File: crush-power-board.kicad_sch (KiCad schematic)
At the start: 0 parts

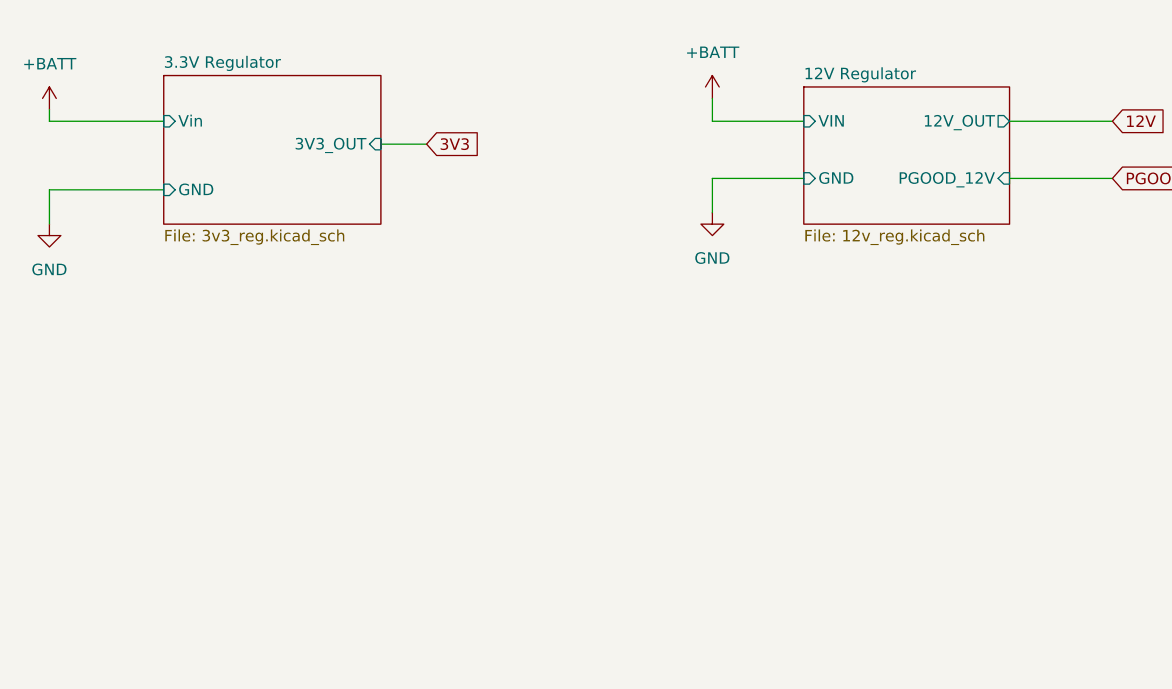
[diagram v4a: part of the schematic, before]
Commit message: Changed 12V Regulator values, added thruster side 3V3 regulator
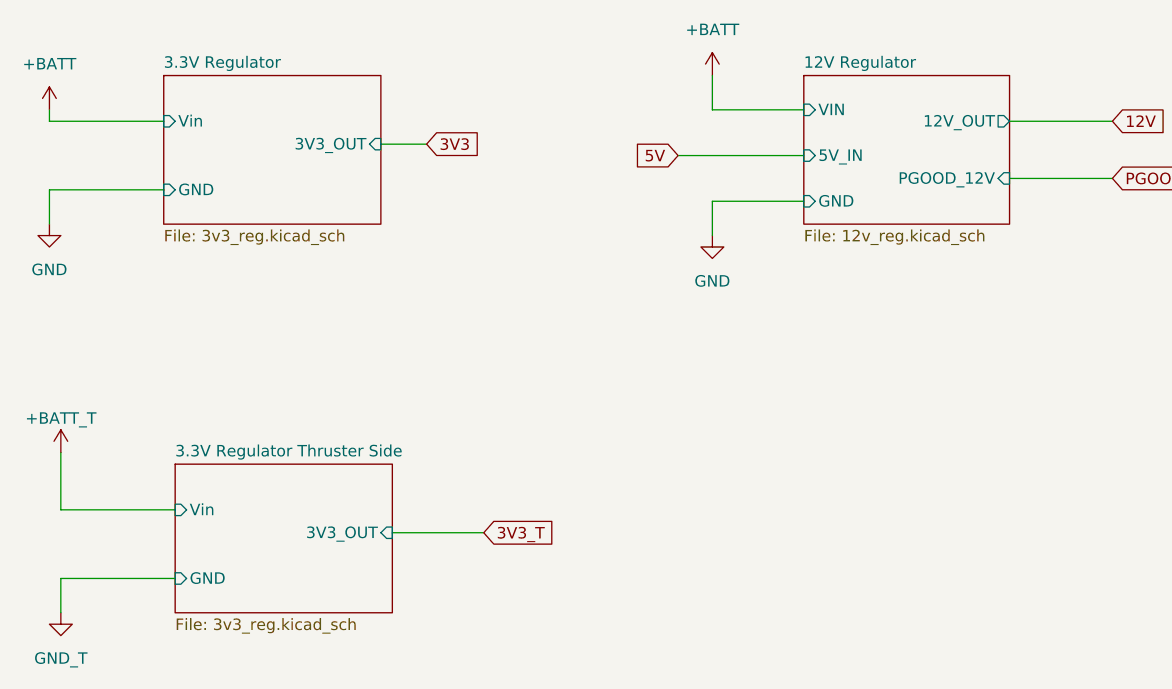
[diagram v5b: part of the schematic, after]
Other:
- added sheet 3.3V Regulator Thruster Side (3v3_reg.kicad_sch)
- sheet 12V Regulator ports: added 5V_IN; removed none
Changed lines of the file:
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@@
     (stroke (width 0) (type default))
   )
-  (wire (pts (xy 142.24 34.29) (xy 132.08 34.29))
+  (wire (pts (xy 142.24 33.02) (xy 132.08 33.02))
     (stroke (width 0) (type default))
   )
@@
     (stroke (width 0) (type default))
   )
-  (wire (pts (xy 132.08 40.64) (xy 132.08 44.45))
+  (wire (pts (xy 59.69 77.47) (xy 72.39 77.47))
+    (stroke (width 0) (type default))
+  )
+  (wire (pts (xy 132.08 43.18) (xy 132.08 46.99))
+    (stroke (width 0) (type default))
+  )
+  (wire (pts (xy 59.69 71.12) (xy 59.69 77.47))
     (stroke (width 0) (type default))
   )
@@
     (stroke (width 0) (type default))
   )
+  (wire (pts (xy 96.52 80.01) (xy 106.68 80.01))
+    (stroke (width 0) (type default))
+  )
+  (wire (pts (xy 59.69 85.09) (xy 59.69 88.9))
+    (stroke (width 0) (type default))
+  )
   (wire (pts (xy 58.42 34.29) (xy 71.12 34.29))
     (stroke (width 0) (type default))
   )
-  (wire (pts (xy 132.08 40.64) (xy 142.24 40.64))
-    (stroke (width 0) (type default))
-  )
-  (wire (pts (xy 132.08 31.75) (xy 132.08 34.29))
+  (wire (pts (xy 132.08 43.18) (xy 142.24 43.18))
+    (stroke (width 0) (type default))
+  )
+  (wire (pts (xy 72.39 85.09) (xy 59.69 85.09))
+    (stroke (width 0) (type default))
+  )
+  (wire (pts (xy 128.27 38.1) (xy 142.24 38.1))
+    (stroke (width 0) (type default))
+  )
+  (wire (pts (xy 132.08 29.21) (xy 132.08 33.02))
     (stroke (width 0) (type default))
   )
@@
     )
   )
+  (global_label "3V3_T" (shape input) (at 106.68 80.01 0) (fields_autoplaced)
+    (effects (font (size 1.27 1.27)) (justify left))
+    (property "Intersheetrefs" "${INTERSHEET_REFS}" (at 115.0286 80.01 0)
+      (effects (font (size 1.27 1.27)) (justify left) hide)
+    )
+  )
   (global_label "3V3" (shape input) (at 100.33 36.83 0) (fields_autoplaced)
     (effects (font (size 1.27 1.27)) (justify left))
@@
     )
   )
+  (global_label "5V" (shape input) (at 128.27 38.1 180) (fields_autoplaced)
+    (effects (font (size 1.27 1.27)) (justify right))
+    (property "Intersheetrefs" "${INTERSHEET_REFS}" (at 123.0661 38.1 0)
+      (effects (font (size 1.27 1.27)) (justify right) hide)
+    )
+  )
   (symbol (lib_id "power:GND") (at 58.42 45.72 0) (unit 1)
     (in_bom yes) (on_board yes) (dnp no) (fields_autoplaced)
@@
     )
   )
-  (symbol (lib_id "power:GND") (at 132.08 44.45 0) (unit 1)
-    (in_bom yes) (on_board yes) (dnp no) (fields_autoplaced)
-    (property "Reference" "#PWR04" (at 132.08 50.8 0)
-      (effects (font (size 1.27 1.27)) hide)
-    )
-    (property "Value" "GND" (at 132.08 49.53 0)
-      (effects (font (size 1.27 1.27)))
-    )
-    (property "Footprint" "" (at 132.08 44.45 0)
-      (effects (font (size 1.27 1.27)) hide)
-    )
-    (property "Datasheet" "" (at 132.08 44.45 0)
+  (symbol (lib_id "power:GND") (at 132.08 46.99 0) (unit 1)
+    (in_bom yes) (on_board yes) (dnp no) (fields_autoplaced)
+    (property "Reference" "#PWR04" (at 132.08 53.34 0)
+      (effects (font (size 1.27 1.27)) hide)
+    )
+    (property "Value" "GND" (at 132.08 52.07 0)
+      (effects (font (size 1.27 1.27)))
+    )
+    (property "Footprint" "" (at 132.08 46.99 0)
+      (effects (font (size 1.27 1.27)) hide)
+    )
+    (property "Datasheet" "" (at 132.08 46.99 0)
       (effects (font (size 1.27 1.27)) hide)
     )
@@
     )
   )
-  (symbol (lib_id "power:+BATT") (at 132.08 31.75 0) (unit 1)
-    (in_bom yes) (on_board yes) (dnp no) (fields_autoplaced)
-    (property "Reference" "#PWR03" (at 132.08 35.56 0)
-      (effects (font (size 1.27 1.27)) hide)
-    )
-    (property "Value" "+BATT" (at 132.08 26.67 0)
-      (effects (font (size 1.27 1.27)))
-    )
-    (property "Footprint" "" (at 132.08 31.75 0)
-      (effects (font (size 1.27 1.27)) hide)
-    )
-    (property "Datasheet" "" (at 132.08 31.75 0)
+  (symbol (lib_id "power:+BATT") (at 132.08 29.21 0) (unit 1)
+    (in_bom yes) (on_board yes) (dnp no) (fields_autoplaced)
+    (property "Reference" "#PWR03" (at 132.08 33.02 0)
+      (effects (font (size 1.27 1.27)) hide)
+    )
+    (property "Value" "+BATT" (at 132.08 24.13 0)
+      (effects (font (size 1.27 1.27)))
+    )
+    (property "Footprint" "" (at 132.08 29.21 0)
+      (effects (font (size 1.27 1.27)) hide)
+    )
+    (property "Datasheet" "" (at 132.08 29.21 0)
       (effects (font (size 1.27 1.27)) hide)
     )
@@
         (path "/530b9f5d-4c5f-47a4-a889-3cce870d311f"
           (reference "#PWR03") (unit 1)
+        )
+      )
+    )
+  )
+  (symbol (lib_id "power:+BATT") (at 59.69 71.12 0) (unit 1)
+    (in_bom yes) (on_board yes) (dnp no) (fields_autoplaced)
+    (property "Reference" "#PWR07" (at 59.69 74.93 0)
+      (effects (font (size 1.27 1.27)) hide)
+    )
+    (property "Value" "+BATT_T" (at 59.69 67.31 0)
+      (effects (font (size 1.27 1.27)))
+    )
+    (property "Footprint" "" (at 59.69 71.12 0)
+      (effects (font (size 1.27 1.27)) hide)
+    )
+    (property "Datasheet" "" (at 59.69 71.12 0)
+      (effects (font (size 1.27 1.27)) hide)
+    )
+    (pin "1")
+    (instances
+      (project "crush-power-board"
+        (path "/530b9f5d-4c5f-47a4-a889-3cce870d311f"
+          (reference "#PWR07") (unit 1)
+        )
+      )
+    )
+  )
+  (symbol (lib_id "power:GND") (at 59.69 88.9 0) (unit 1)
+    (in_bom yes) (on_board yes) (dnp no) (fields_autoplaced)
+    (property "Reference" "#PWR08" (at 59.69 95.25 0)
+      (effects (font (size 1.27 1.27)) hide)
+    )
+    (property "Value" "GND_T" (at 59.69 93.98 0)
+      (effects (font (size 1.27 1.27)))
+    )
+    (property "Footprint" "" (at 59.69 88.9 0)
+      (effects (font (size 1.27 1.27)) hide)
+    )
+    (property "Datasheet" "" (at 59.69 88.9 0)
+      (effects (font (size 1.27 1.27)) hide)
+    )
+    (pin "1")
+    (instances
+      (project "crush-power-board"
+        (path "/530b9f5d-4c5f-47a4-a889-3cce870d311f"
+          (reference "#PWR08") (unit 1)
         )
       )
@@
     )
   )
-  (sheet (at 142.24 30.48) (size 22.86 15.24) (fields_autoplaced)
+  (sheet (at 142.24 29.21) (size 22.86 16.51) (fields_autoplaced)
     (stroke (width 0.1524) (type solid))
     (fill (color 0 0 0 0.0000))
-    (property "Sheetname" "12V Regulator" (at 142.24 29.7684 0)
+    (property "Sheetname" "12V Regulator" (at 142.24 28.4984 0)
       (effects (font (size 1.27 1.27)) (justify left bottom))
     )
@@
       (effects (font (size 1.27 1.27)) (justify right))
     )
-    (pin "GND" input (at 142.24 40.64 180)
-      (effects (font (size 1.27 1.27)) (justify left))
-    )
-    (pin "VIN" input (at 142.24 34.29 180)
+    (pin "GND" input (at 142.24 43.18 180)
+      (effects (font (size 1.27 1.27)) (justify left))
+    )
+    (pin "VIN" input (at 142.24 33.02 180)
       (effects (font (size 1.27 1.27)) (justify left))
     )
@@
       (effects (font (size 1.27 1.27)) (justify right))
     )
+    (pin "5V_IN" input (at 142.24 38.1 180)
+      (effects (font (size 1.27 1.27)) (justify left))
+    )
     (instances
       (project "crush-power-board"
@@
       )
     )
+  )
+  (sheet (at 72.39 72.39) (size 24.13 16.51) (fields_autoplaced)
+    (stroke (width 0.1524) (type solid))
+    (fill (color 0 0 0 0.0000))
+    (property "Sheetname" "3.3V Regulator Thruster Side" (at 72.39 71.6784 0)
+      (effects (font (size 1.27 1.27)) (justify left bottom))
+    )
+    (property "Sheetfile" "3v3_reg.kicad_sch" (at 72.39 89.4846 0)
+      (effects (font (size 1.27 1.27)) (justify left top))
+    )
+    (pin "GND" input (at 72.39 85.09 180)
+      (effects (font (size 1.27 1.27)) (justify left))
+    )
+    (pin "Vin" input (at 72.39 77.47 180)
+      (effects (font (size 1.27 1.27)) (justify left))
+    )
+    (pin "3V3_OUT" input (at 96.52 80.01 0)
+      (effects (font (size 1.27 1.27)) (justify right))
+    )
+    (instances
+      (project "crush-power-board"
+        (path "/530b9f5d-4c5f-47a4-a889-3cce870d311f" (page "5"))
+      )
+    )

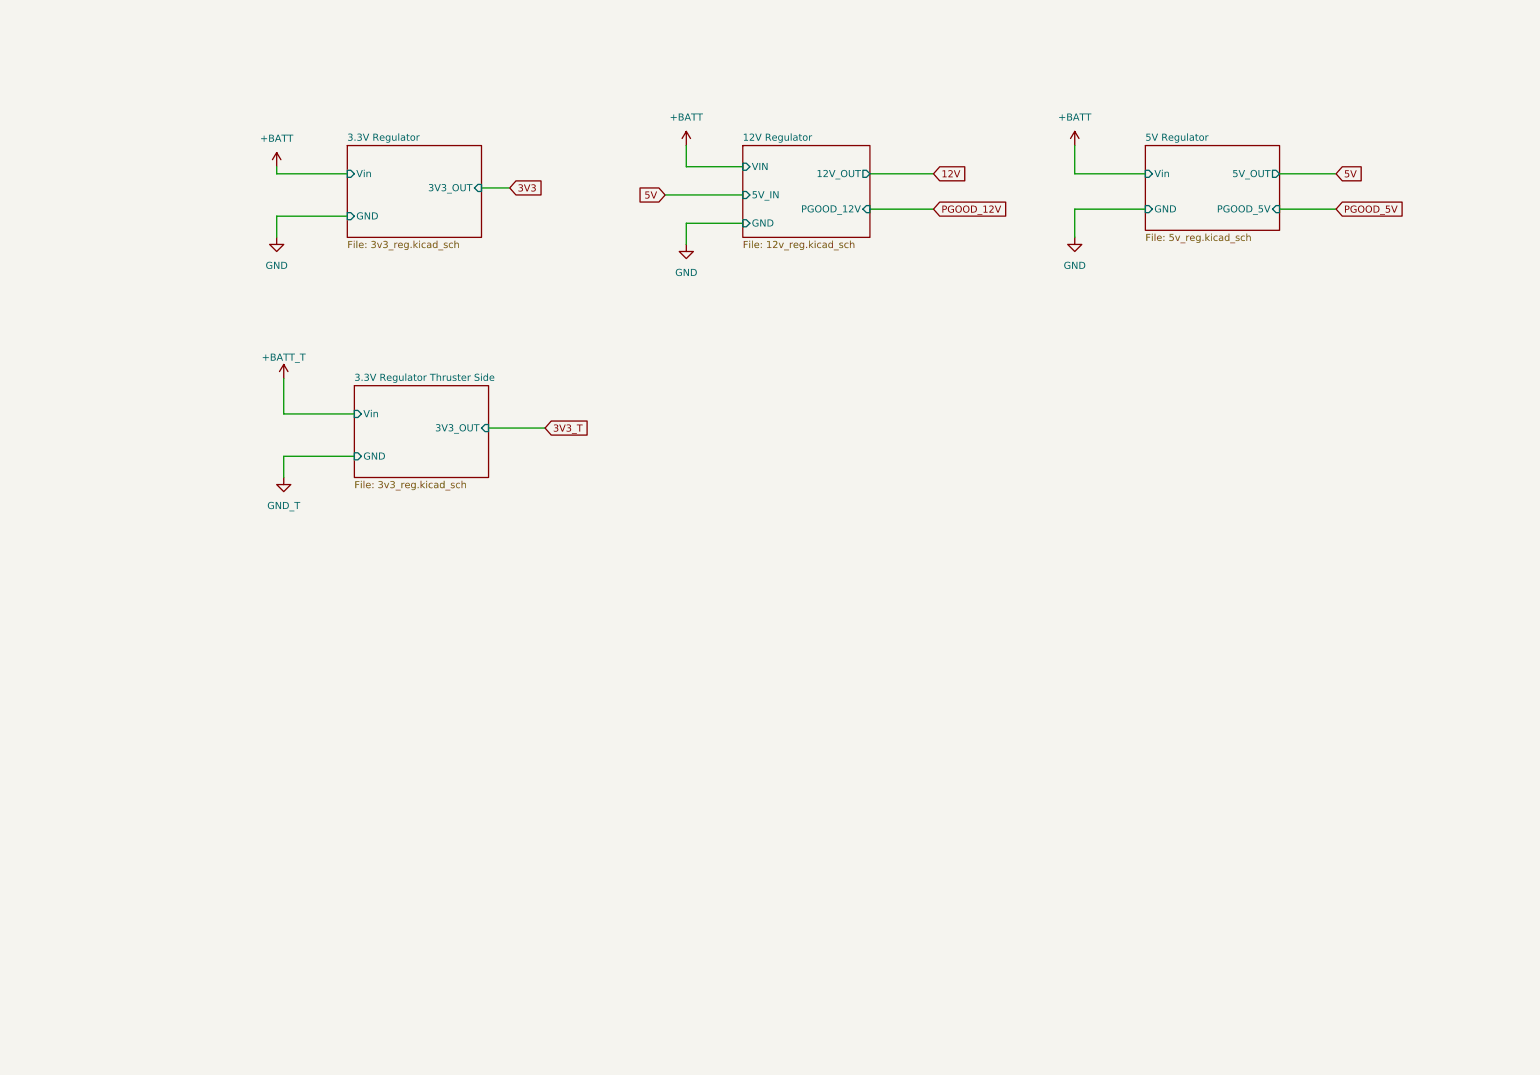
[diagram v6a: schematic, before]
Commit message: Added indicator LEDs and fixed some footprints
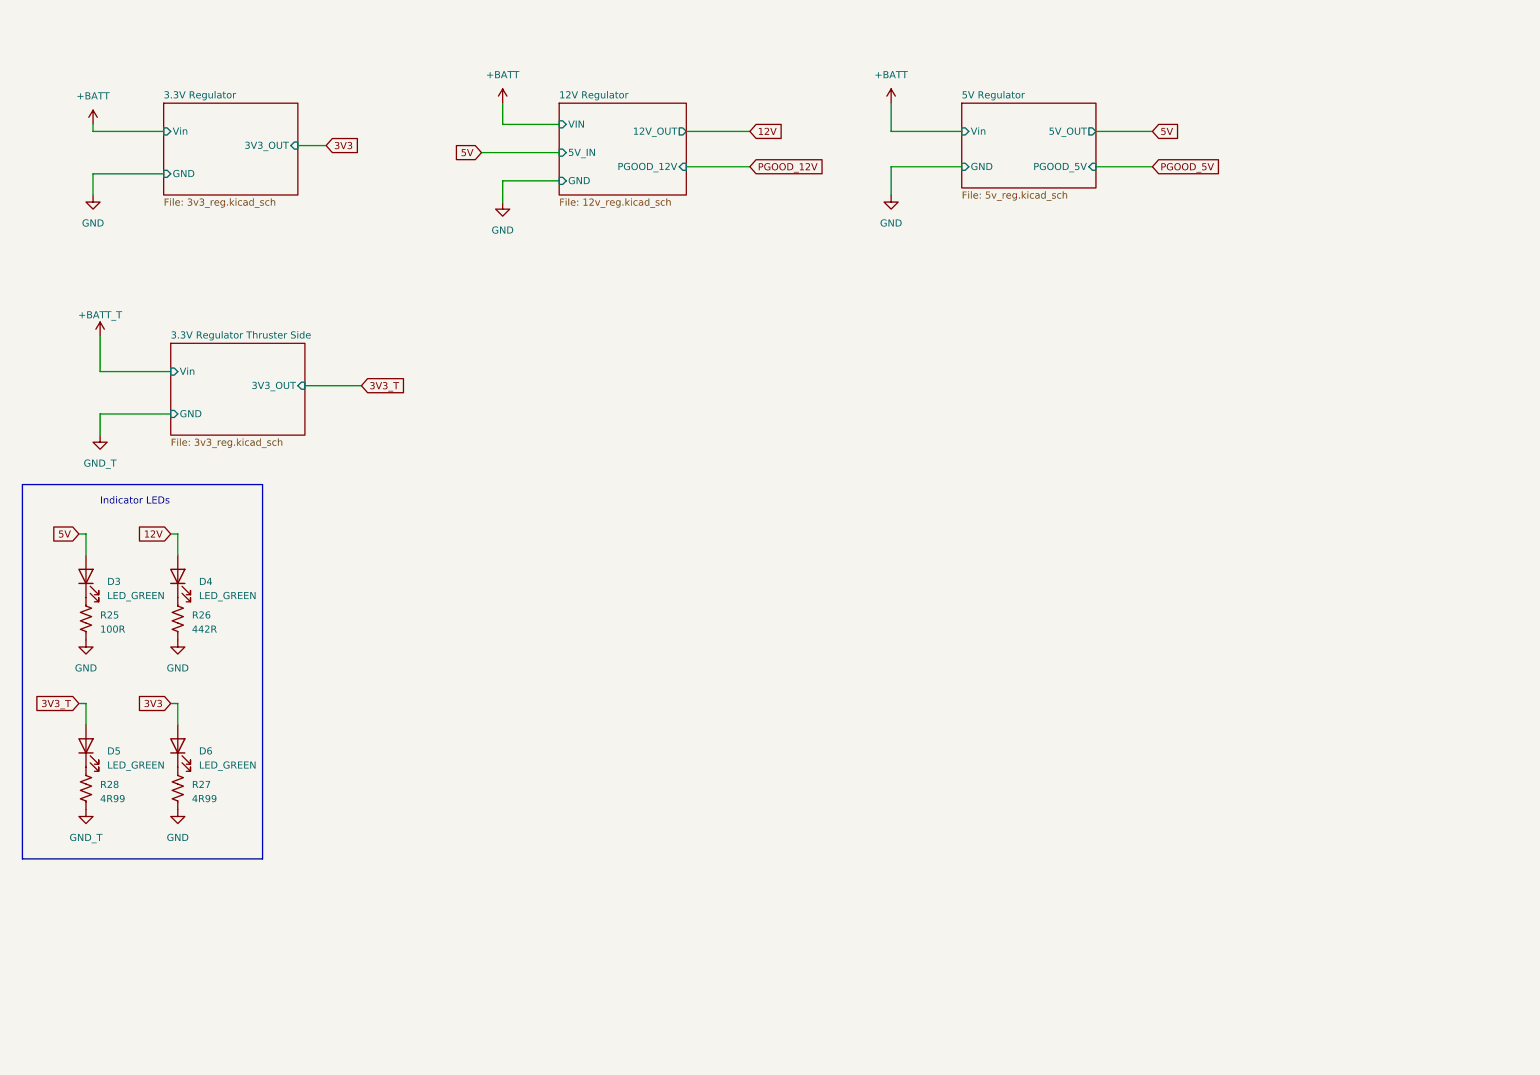
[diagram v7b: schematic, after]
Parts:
- added D3, D4, D5, D6: LED_GREEN, LED_SMD:LED_0603_1608Metric, symbol Device:LED
- added R25: 100R, Resistor_SMD:R_0603_1608Metric, symbol Device:R_US
- added R26: 442R, Resistor_SMD:R_0603_1608Metric, symbol Device:R_US
- added R27, R28: 4R99, Resistor_SMD:R_0603_1608Metric, symbol Device:R_US
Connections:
- net 12V: now also D4.2 (A)
- net 3V3: now also D6.2 (A)
- net 3V3_T: now also D5.2 (A)
- net 5V: now also D3.2 (A)
- net GND: now also R25.2, R26.2, R27.2, R28.2
- new net: D3.1 (K), R25.1
- new net: D5.1 (K), R28.1
- new net: D6.1 (K), R27.1
- new net: D4.1 (K), R26.1
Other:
- note added: "Indicator LEDs"
